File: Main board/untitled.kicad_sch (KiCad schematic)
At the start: 53 parts, among them J1 RPi, J10 RA, J11 EL, J12 AZ, J13 GPS, J14 SHUTTER, J15 PWR_ON, J2 RJE05-166-1310, J9 DEC, Q1 2N7002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

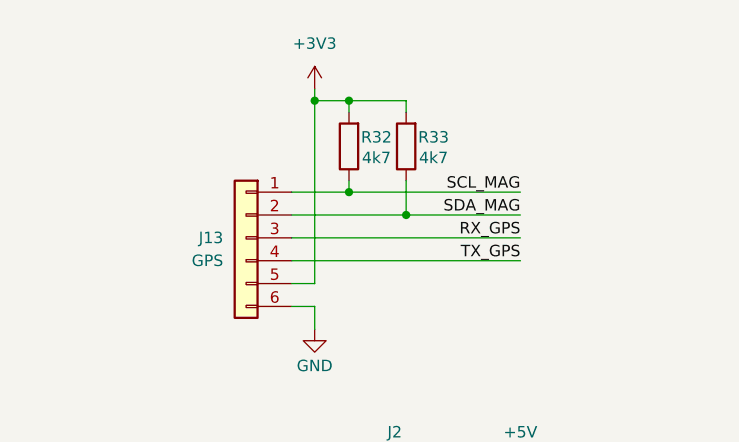
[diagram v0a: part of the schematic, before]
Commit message: Updated V1.0 schematic values
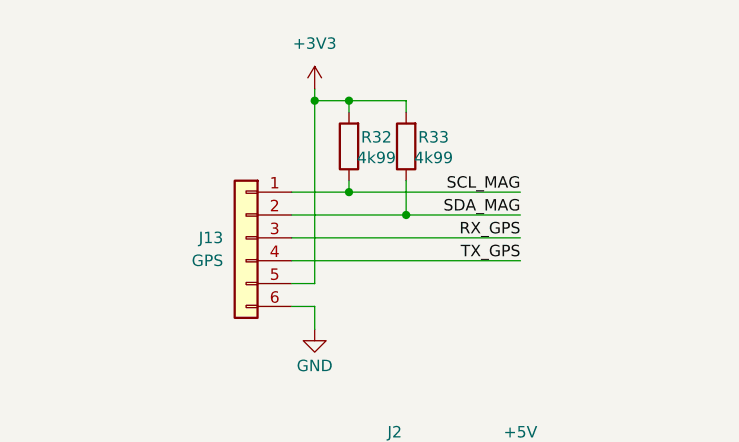
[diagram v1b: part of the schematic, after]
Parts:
- R32, R33: value 4k7 -> 4k99
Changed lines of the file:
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@@
 			)
 		)
-		(property "Value" "4k7"
+		(property "Value" "4k99"
 			(at 248.158 36.83 0)
 			(effects
@@
 			)
 		)
-		(property "Value" "4k7"
+		(property "Value" "4k99"
 			(at 241.808 36.83 0)
 			(effects

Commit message: Tracking logic updated
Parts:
- R41, R42: value 2k2 -> 0R
- R43, R44: value 2k2 -> 1k
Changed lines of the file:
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@@
 			)
 		)
-		(property "Value" "2k2"
+		(property "Value" "0R"
 			(at 45.72 155.194 90)
 			(effects
@@
 			)
 		)
-		(property "Value" "2k2"
+		(property "Value" "1k"
 			(at 76.2 167.894 90)
 			(effects
@@
 			)
 		)
-		(property "Value" "2k2"
+		(property "Value" "1k"
 			(at 76.2 155.194 90)
 			(effects
@@
 			)
 		)
-		(property "Value" "2k2"
+		(property "Value" "0R"
 			(at 45.72 167.894 90)
 			(effects
